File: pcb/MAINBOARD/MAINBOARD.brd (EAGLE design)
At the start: 85 x 56 mm, 67 parts, among them Q1 20MHz, SW1 P-DT6E, SW2 P-DT6E, T1 IRMLM0060TRPbF

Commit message: Přidány opravy chyb, které se vyskytly během oživování
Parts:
- added C10, C7: 100n, !discrete:0805
- added C8, C9: 1n, !discrete:0805
- added D7: 1N4148, #PaJa_30:SOD-80
- added R20, R21: 100k, !discrete:0805
- C1, C3: value 100uF/16V -> 100uF
- D2, D3, D4, D5, D6: device led:CHIPLED_0805 -> !opto:LED_0805
- DC1: value DC-DC-STEPDOWN -> MP1584
- DZ1: value D -ZENEROVA 3.3V -> BZV55C3.3
- DZ2: value D-ZENEROVA 3.3V -> BZV55C3.3
- R1, R11, R12, R2, R3, R4, R7, R8: device rcl:R0603 -> !discrete:0805
- R10, R14, R16, R17, R18, R19: value 68R -> 330R
- R5: device rcl:M1206 -> !discrete:1206
- R6, R9: value DNP -> 10k
- T1: device transistor:SOT23-EBC -> #TD:NPN-BCE
- moved R10 25.4 mm to (38.1, 20.3), flipped to the top
- moved D1 22.9 mm to (35.6, 20.3), flipped to the top, turned to 90 degrees
- moved R15 3.86 mm to (76.8, 25.4), turned to 180 degrees
- moved C4 3.18 mm to (51.4, 8.89)
- moved C6 2.62 mm to (55.9, 9.53), turned to 180 degrees
- moved R1 1.91 mm to (55.2, 21.6)
- moved R11 1.42 mm to (55.9, 12.1)
- moved D3 1.30 mm to (43.8, 2.92), turned to 0 degrees
- moved D4 1.30 mm to (39.4, 2.92), turned to 0 degrees
- moved D5 1.30 mm to (34.9, 2.92), turned to 0 degrees
- moved D6 1.30 mm to (48.3, 2.92), turned to 0 degrees
- moved D2 1.30 mm to (30.5, 2.92), turned to 0 degrees
- moved R7 1.27 mm to (55.9, 26.7)
- moved T1 0.90 mm to (78.7, 29.2)
- moved B1 0.90 mm to (78.7, 45.7)
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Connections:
- net N$2 renamed B
- removed net N$13: D3.C, R17.2
- removed net N$15: D5.C, R18.2
- removed net N$9: D2.C, R16.2
- new net C: D7.A, SG1.-, T1.C
- new net N$2: D6.A, R19.2
- new net N$7: D2.A, R16.2
- net +3V3: now also C10.2, C9.2, R20.2, R21.2; no longer D2.A, D3.A, D4.A, D5.A, D6.A, SG1.+
- net +5V: now also C7.1, C8.1, D7.K, SG1.+
- net AGND: no longer D1.K
- net GND: now also C10.1, C7.2, C8.2, C9.1, D1.K, D2.K, D3.K, D4.K, D5.K, D6.K
- net GPB5-2: now also R20.1
- net GPB6-2: now also R21.1
- net N$3: now also D3.A, R17.2; no longer SG1.-, T1.C
- net N$4: now also D4.A, R14.2; no longer D6.C, R19.2
- net N$6: now also D5.A, R18.2; no longer D4.C, R14.2
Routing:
- net GND: track 64.3 -> 119.3 mm, vias 7 -> 10
- net +5V: track 162.8 -> 211.3 mm
- net C: track 0.00 -> 8.83 mm
- net GPB7-2: track 86.9 -> 78.2 mm
- net VBATT: track 75.7 -> 70.8 mm
- net N$15: track 3.02 -> 0.00 mm
- net N$9: track 3.02 -> 0.00 mm
- net N$13: track 3.02 -> 0.00 mm
- net XTAL2: track 9.72 -> 12.5 mm
- net N$23: track 2.54 -> 5.08 mm
- net +3V3: track 49.1 -> 51.7 mm, vias 2 -> 4
- net XTAL1: track 6.91 -> 9.27 mm
- net N$3: track 4.41 -> 2.16 mm
- net N$7: track 0.00 -> 2.16 mm
- net N$2: track 0.00 -> 2.16 mm
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
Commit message: Velke upravy pred odeslanim do seriove vyroby
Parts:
- removed DZ1, DZ2: BZV55C3.3, #PaJa_22:SOD-80
- removed T1: IRMLM0060TRPbF, #TD:NPN-BCE
- added D8: BZV55C3.3, !discrete:D_SOD80
- added D9: BZV55V3.3, !discrete:D_SOD80
- added T2: (no value), !transistor:SOT23
- D7: value 1N4148 -> LL4148; device #PaJa_30:SOD-80 -> !diody:D_SOD80
- moved C7 3.42 mm to (33.0, 40.0)
- moved C8 2.01 mm to (31.1, 40.0), turned to 90 degrees
- moved R15 1.91 mm to (78.7, 25.4)
- moved JP25 0.76 mm to (6.99, 21.5)
- moved R1 0.64 mm to (55.9, 21.6)
- moved R2 0.63 mm to (62.2, 21.6)
- moved JP26 0.38 mm to (6.99, 16.1)
- moved Q1 0.38 mm to (53.6, 6.99)
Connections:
- net +5V: now also D7.C; no longer D7.K
- net B: now also T2.1; no longer T1.B
- net C: now also T2.2; no longer T1.C
- net GND: now also D8.A, D9.A, T2.3; no longer DZ1.A, DZ2.A, T1.E
- net SCL: now also D9.C; no longer DZ2.K
- net SDA: now also D8.C; no longer DZ1.K
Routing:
- net SDA: track 118.9 -> 121.5 mm, vias 4 -> 3
- net SCL: track 122.2 -> 124.3 mm
- net GPB7-2: track 78.2 -> 80.1 mm
- net B: track 4.29 -> 3.03 mm
- net TRIG1-PD5-OC0B: track 16.7 -> 15.6 mm
- net +5V: track 211.3 -> 210.3 mm
- net N$5: track 2.54 -> 1.91 mm
- added copper zone on layer 1, net GND
- added copper zone on layer 1, net N$12
- added copper zone on layer 1, net N$16

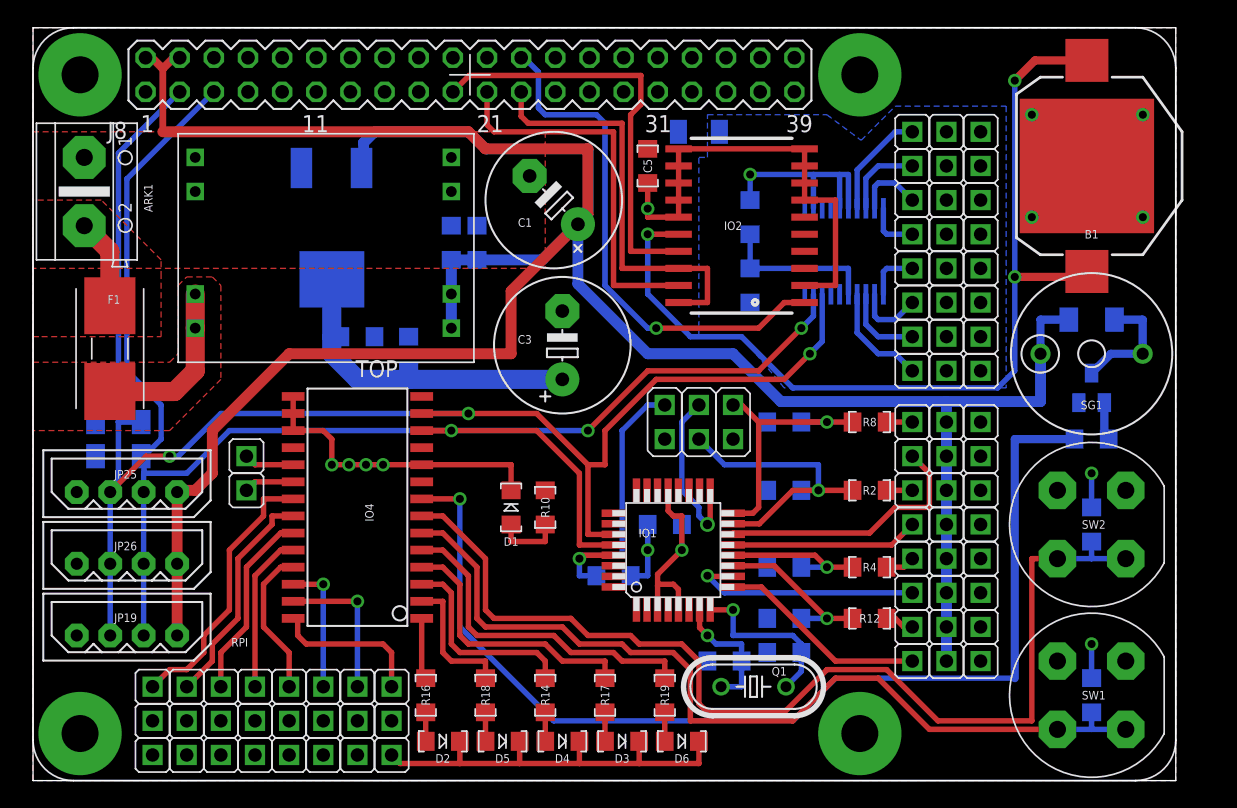
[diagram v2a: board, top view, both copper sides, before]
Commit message: New version of board, shipped to SeedStudio (2x KM2-B, 1x Mainboard -A)
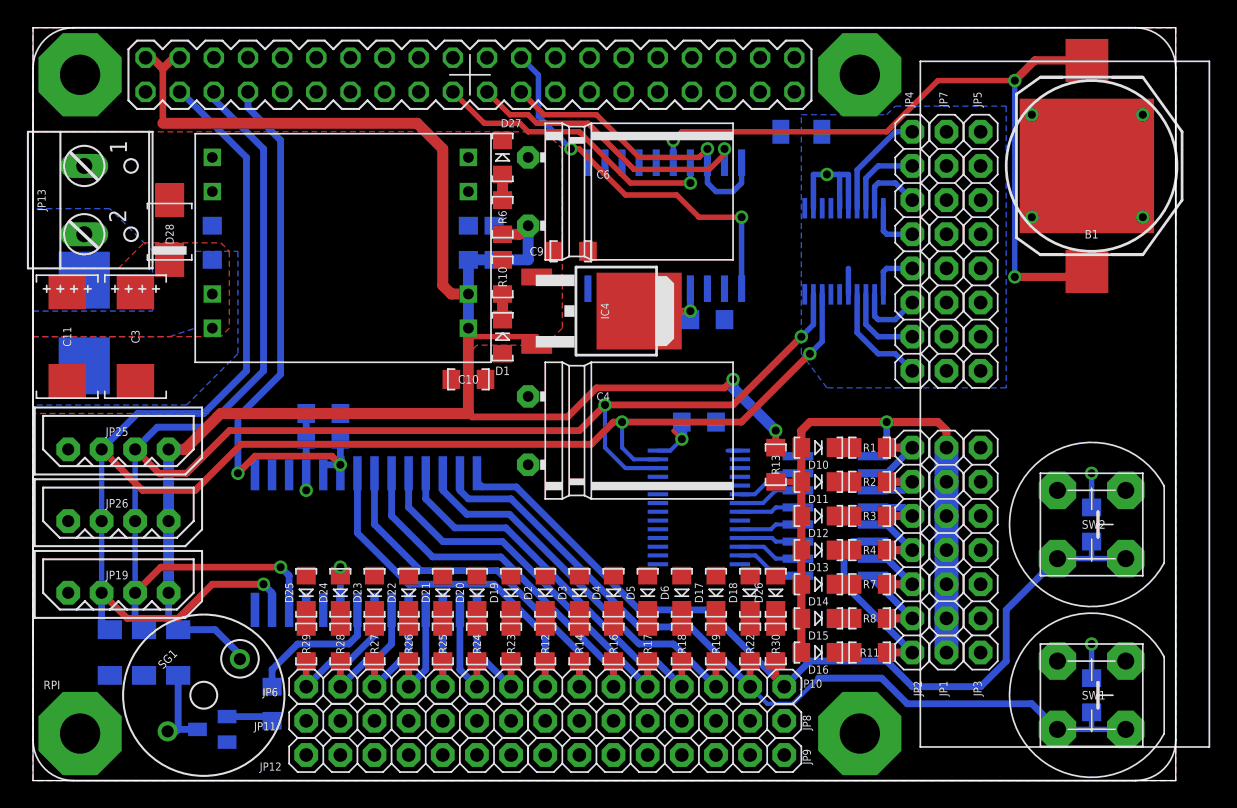
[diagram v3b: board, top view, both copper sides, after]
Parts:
- removed ARK1: ARK500/2, #TD:ARK500/2
- removed IO1: ATmega88PA-AU, !ic_avr:TQFP32
- removed IO4: MCP23017SO, microchip:SO28W
- removed IO5: LD1086, #TD:DPACK
- removed JP14, JP23, JP24, JP28, JP29: S1G8_JUM, #Lamacie lišty by TD:8
- removed Q1: 20MHz, crystal:HC49/S
- added C11: 22M, !discrete:CT7343D
- added C12: 100n, !discrete:0805
- added D10, D11, D12, D13, D14, D15, D16, D17, D18, D19, D20, D21, D22, D23, D24, D25, D26, D27: KP-2012SGC, !opto:LED_0805
- added D28: SK24, !discrete:D_SMB
- added IC1: PCA9685, !ic_nxp:TSSOP28
- added IC2: MCP23017/SO, !ic_microchip:SO28W
- added IC3: ULN2003D1013TR, !uln:SO16
- added IC4: LD1086DT33, !stab:TO252
- added JP12: DS1021-1*8SF1-1, !pinhead:1X07_254_M
- added JP13: TB-5.08-P-2P/BL, !pinhead:1X02_508_SROUB
- added R22, R23, R24, R25, R26, R27, R28, R29, R30: 330, !discrete:0805
- added U$39: (no value), !frames:DIN_A4_SCALE2
- added U$48: (no value), !frames:DIN_DOCFIELD_SCALE2
- C1: value 100uF -> 100n; device rcl:E5-10,5 -> !discrete:0805
- C3: value 100uF -> 22M; device rcl:E5-10,5 -> !discrete:CT7343D
- C4: value 22p -> 1000M; device !discrete:0805 -> !discrete:CE_D10L13_L
- C6: value 22p -> 1000M; device !discrete:0805 -> !discrete:CE_D10L13_R
- D2, D4, D5: value G -> KP-2012SGC
- D3: value O -> KP-2012SGC
- D6: value R -> KP-2012SGC
- D8: value BZV55C3.3 -> BZV55C3V3
- D9: value BZV55V3.3 -> BZV55C3V3
- JP1: value S2G3_JUM -> DS1021-1*8SF1-1; device #Lamacie lišty by TD:2X3 -> !pinhead:1X07_254_M
- JP10, JP4, JP7, JP8, JP9: value S1G3_JUM -> DS1021-1*8SF1-1; device #Lamacie lišty by TD:3 -> !pinhead:1X08_254_M
- JP11, JP2, JP3: value S1G3_JUM -> DS1021-1*8SF1-1; device #Lamacie lišty by TD:3 -> !pinhead:1X07_254_M
- JP5: value S1G8_JUM -> DS1021-1*8SF1-1; device #Lamacie lišty by TD:8 -> !pinhead:1X08_254_M
- JP6: value S1G2_JUM -> DS1021-1*8SF1-1; device #Lamacie lišty by TD:2 -> !pinhead:1X07_254_M
- R1, R11, R3, R7: value 470R -> 330
- R10, R12, R14, R16, R17, R18, R19, R2, R4, R8: value 330R -> 330
- R13: value 10k -> *
- R6: value 10k -> 330
- R9: value 10k -> 100k
- T2: value (none) -> IRLML0060
- moved D7 72.3 mm to (10.8, 9.53), turned to 270 degrees
- moved SG1 70.8 mm to (12.7, 6.35), turned to 45 degrees
- moved T2 70.2 mm to (13.3, 3.81), turned to 270 degrees
- moved R15 64.1 mm to (17.8, 5.71), turned to 270 degrees
- moved JP11 45.8 mm to (27.9, 4.45), turned to 0 degrees
- moved C6 39.2 mm to (36.8, 43.8), flipped to the top, turned to 0 degrees
- moved R9 35.8 mm to (21.6, 25.4), turned to 180 degrees
- moved C3 31.8 mm to (7.62, 33.0), turned to 270 degrees
- moved JP9 30.5 mm to (47.0, 1.91)
- moved C1 25.6 mm to (13.3, 40.0), flipped to the bottom, turned to 90 degrees
- moved JP10 25.5 mm to (47.0, 6.99)
- moved JP8 25.5 mm to (47.0, 4.45)
- moved JP4 25.5 mm to (65.4, 39.4), turned to 90 degrees
- moved R12 24.2 mm to (38.1, 10.2), turned to 90 degrees
- moved JP7 22.9 mm to (67.9, 39.4), turned to 90 degrees
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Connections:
- removed net ECHO1-PD7: IO1.11, R11.2, R12.2
- removed net ECHO2-PB0: IO1.12, R3.2, R4.2
- removed net ECHO3-PB3: IO1.15, JP1.2, R1.2, R2.2
- removed net ECHO4-PB4: IO1.16, JP1.6, R7.2, R8.2
- removed net GPA0-2: IO4.21, JP14.1
- removed net GPA1-2: IO4.22, JP14.2
- removed net GPA2-2: IO4.23, JP14.3
- removed net GPA3-2: IO4.24, JP14.4
- removed net GPA4-2: IO4.25, JP14.5
- removed net GPA5-2: IO4.26, JP14.6
- removed net GPA6-2: IO4.27, JP14.7
- removed net GPA7-2: IO4.28, JP14.8
- removed net GPB0-2: IO4.1, R16.1
- removed net GPB1-2: IO4.2, R18.1
- removed net GPB2-2: IO4.3, R14.1
- removed net GPB3-2: IO4.4, R17.1
- removed net GPB4-2: IO4.5, R19.1
- removed net GPB5-2: IO4.6, R20.1, SW1.2, SW1.2A
- removed net GPB6-2: IO4.7, R21.1, SW2.2, SW2.2A
- removed net GPB7-2: IO4.8, R15.1
- removed net INT/SQW: IO2.5
- removed net INTA1: IO4.20, JP6.2
- removed net INTB1: IO4.19, JP6.1
- removed net N$1: JP11.3, R8.1
- removed net N$11: JP3.3, R12.1
- removed net N$23: D1.A, R10.1
- removed net N$5: JP10.3, R2.1
- removed net N$8: JP7.3, R4.1
- removed net RESET: IO1.29, JP1.4, R13.2
- removed net SCK: IO1.17, JP1.5
- removed net TRIG1-PD5-OC0B: IO1.9, JP2.1
- removed net TRIG2-PD6-OC0A: IO1.10, JP4.1
- removed net TRIG3-PB1-OC1A: IO1.13, JP8.1
- removed net TRIG4-PB2-OC1B: IO1.14, JP9.1
- removed net XTAL1: C4.2, IO1.7, Q1.2
- removed net XTAL2: C6.2, IO1.8, Q1.1
- new net INT: IC2.19, IC2.20, R9.2, RPI.7
- new net LED0: IC1.6, IC3.7
- new net N$17: IC1.7, IC3.6
- new net N$18: D10.A, D11.A, D12.A, D13.A, D14.A, D15.A, D16.A, IC3.9, JP1.1, JP1.2, JP1.3, JP1.4, JP1.5, JP1.6, JP1.7, R13.2
- new net N$19: IC1.8, IC3.5
- new net N$20: D10.K, R1.2
- new net N$21: D16.K, R11.2
- new net N$24: IC1.10, IC3.4
- new net N$25: IC1.11, IC3.3
- new net N$26: IC1.12, IC3.2
- new net N$27: IC1.13, IC3.1
- new net N$28: D15.K, R8.2
- new net N$29: D14.K, R7.2
- new net N$30: D13.K, R4.2
- new net N$31: D12.K, R3.2
- new net N$32: D11.K, R2.2
- new net N$33: D5.K, R17.2
- new net N$34: D4.K, R16.2
- new net N$35: D3.K, R14.2
- new net N$37: D19.K, R23.2
- new net N$38: D25.K, R29.2
- new net N$39: D24.K, R28.2
- new net N$40: D23.K, R27.2
- new net N$41: D22.K, R26.2
- new net N$42: D21.K, R25.2
- new net N$43: D20.K, R24.2
- new net N$9: D27.A, R6.1
- new net PA0: IC2.21, JP10.8, R12.1
- new net PA1: IC2.22, JP10.7, R14.1
- new net PA2: IC2.23, JP10.6, R16.1
- new net PA3: IC2.24, JP10.5, R17.1
- new net PA4: IC2.25, JP10.4, R18.1
- new net PA5: IC2.26, JP10.3, R19.1
- new net PA6: IC2.27, JP10.2, R20.1, R22.1, SW1.2, SW1.2A
- new net PA7: IC2.28, JP10.1, R21.1, R30.1, SW2.2, SW2.2A
- new net PB0: IC2.1, JP6.7, R23.1
- new net PB1: IC2.2, JP6.6, R24.1
- new net PB2: IC2.3, JP6.5, R25.1
- new net PB3: IC2.4, JP6.4, R26.1
- new net PB4: IC2.5, JP6.3, R27.1
- new net PB5: IC2.6, JP6.2, R28.1
- new net PB6: IC2.7, JP6.1, R29.1
- new net PB7: IC2.8, R15.1
- new net PWM0: IC3.10, JP2.1, R1.1
- new net PWM1: IC3.11, JP2.2, R2.1
- new net PWM2: IC3.12, JP2.3, R3.1
- new net PWM4: IC3.13, JP2.4, R4.1
- new net PWM5: IC3.14, JP2.7, R11.1
- new net PWM6: IC3.15, JP2.5, R7.1
- new net PWM7: IC3.16, JP2.6, R8.1
- net +3V3: now also C12.1, C4.P, D1.A, D17.A, D18.A, D19.A, D2.A, D20.A, D21.A, D22.A, D23.A, D24.A, D25.A, D26.A, D3.A, D4.A, D5.A, D6.A, IC1.28, IC2.18, IC2.9, IC4.3, JP11.1, JP11.2, JP11.3, JP11.4, JP11.5, JP11.6, JP11.7, JP7.1, JP7.2, JP7.3, JP7.4, JP7.5, JP7.6, JP7.7, JP7.8, JP8.1, JP8.2, JP8.3, JP8.4, JP8.5, JP8.6, JP8.7, JP8.8, R9.1; no longer C3.+, IO1.1, IO1.18, IO1.19, IO1.2, IO1.20, IO1.22, IO1.23, IO1.24, IO1.25, IO1.26, IO1.30, IO1.31, IO1.32, IO1.4, IO1.6, IO4.18, IO4.9, IO5.4, JP1.3, JP24.1, JP24.2, JP24.3, JP24.4, JP24.5, JP24.6, JP24.7, JP24.8, JP29.1, JP29.2, JP29.3, JP29.4, JP29.5, JP29.6, JP29.7, JP29.8, R10.2, R13.1, R9.2
- net +5V: now also C6.P, IC4.2, R13.1, R6.2; no longer C1.+, IO5.3, JP10.2, JP11.2, JP2.2, JP3.2, JP4.2, JP7.2, JP8.2, JP9.2
- net AD0: now also JP4.8; no longer JP5.1
- net AD1: now also JP4.1; no longer JP5.8
- net AD2: now also JP4.7; no longer JP5.2
- net AD3: now also JP4.2; no longer JP5.7
- net AD4: now also JP4.6; no longer JP5.3
- net AD5: now also JP4.3; no longer JP5.6
- net AD6: now also JP4.5; no longer JP5.4
- net AD7: now also JP4.4; no longer JP5.5
- net AGND: now also IO3.15, JP5.1, JP5.2, JP5.3, JP5.4, JP5.5, JP5.6, JP5.7, JP5.8; no longer JP28.1, JP28.2, JP28.3, JP28.4, JP28.5, JP28.6, JP28.7, JP28.8, R6.2
- net GND: now also C1.2, C11.-, C12.2, C4.M, C6.M, D27.K, D28.A, IC1.1, IC1.14, IC1.2, IC1.23, IC1.24, IC1.25, IC1.3, IC1.4, IC1.5, IC2.10, IC2.15, IC2.16, IC2.17, IC3.8, IC4.1, JP12.1, JP12.2, JP12.3, JP12.4, JP12.5, JP12.6, JP12.7, JP13.1, JP3.2, JP3.3, JP3.4, JP3.5, JP3.6, JP3.7, JP9.1, JP9.2, JP9.4, JP9.5, JP9.6, JP9.7, JP9.8, R10.1; no longer ARK1.1, C1.-, C4.1, C6.1, D1.K, D2.K, D3.K, D4.K, D5.K, D6.K, IO1.21, IO1.3, IO1.5, IO4.10, IO4.15, IO4.16, IO4.17, IO5.1, JP1.1, JP10.1, JP11.1, JP2.3, JP23.1, JP23.2, JP23.3, JP23.4, JP23.5, JP23.6, JP23.7, JP23.8, JP4.3, JP7.1, JP8.3, R1.1, R11.1, R3.1, R7.1
- net N$12: now also C1.1, C11.+, C3.+, D28.K
- net N$16: now also JP13.2; no longer ARK1.2
- net N$2: now also D26.K, R30.2; no longer D6.A, R19.2
- net N$22: now also D1.K, R10.2; no longer IO3.15, R6.1, R9.1
- net N$3: now also D2.K, R12.2; no longer D3.A, R17.2
- net N$4: now also D18.K, R22.2; no longer D4.A, R14.2
- net N$6: now also D17.K, R19.2; no longer D5.A, R18.2
- net N$7: now also D6.K, R18.2; no longer D2.A, R16.2
- net SCL: now also IC1.26, IC2.12; no longer IO1.28, IO4.12
- net SDA: now also IC1.27, IC2.13; no longer IO1.27, IO4.13
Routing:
- net GND: track 119.3 -> 16.4 mm, vias 10 -> 4
- net GPB7-2: track 80.1 -> 0.00 mm, vias 1 -> 0
- net GPB6-2: track 78.7 -> 0.00 mm
- net +5V: track 210.3 -> 137.7 mm, vias 0 -> 2
- net GPB5-2: track 66.8 -> 0.00 mm
- net PA7: track 0.00 -> 66.4 mm
- net PA6: track 0.00 -> 62.9 mm
- net N$18: track 0.00 -> 49.8 mm, vias 0 -> 1
- net INT: track 0.00 -> 43.5 mm, vias 0 -> 2
- net PA5: track 0.00 -> 29.5 mm
- net PA4: track 0.00 -> 28.6 mm
- net PA3: track 0.00 -> 27.7 mm
- net PA2: track 0.00 -> 27.6 mm
- net PA1: track 0.00 -> 27.4 mm
- net PA0: track 0.00 -> 27.3 mm
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- added copper zone on layer 16, net N$12
- added copper zone on layer 16, net N$16
- removed copper zone on layer 1, net N$16
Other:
- board text added: "(c) Frantisek Burian"
- board text added: "(c) Tadeas Divacky"
- board text added: "+"
- board text added: "+5V"
- board text added: "-"
- board text added: "2017"
- board text added: "BRNO"
- board text added: "Brno University of Technology"
- board text added: "FEKT"
- board text added: "GND"
- board text added: "KAMbot"
- board text added: "Main driver board"
- board text added: "PA0"
- board text added: "PA1"
- board text added: "PA2"
- board text added: "PA3"
- board text added: "PA4"
- board text added: "PA5"
- board text added: "PA6"
- board text added: "PA7"
- board text added: "PB0"
- board text added: "PB1"
- board text added: "PB2"
- board text added: "PB3"
- board text added: "PB4"
- board text added: "PB5"
- board text added: "PB6"
- board text added: "PB7"
- board text added: "PWM0"
- board text added: "PWM1"
- board text added: "PWM2"
- board text added: "PWM4"
- board text added: "PWM5"
- board text added: "PWM6"
- board text added: "PWM7"
- board text added: "SCL"
- board text added: "SDA"
- board text added: "UAMT"
- board text added: "UAMT FEKT VUT"
- board text added: "rev A"
- board text removed: "B5"
- board text removed: "B6"
- board text removed: "B7"

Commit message: KM2 a MAINBOARD - posledni upravy pred Release
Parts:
- removed IO2: DS3234, SparkFun:DS3234
- removed U$39: (no value), !frames:DIN_A4_SCALE2
- removed U$48: (no value), !frames:DIN_DOCFIELD_SCALE2
- added IC5: DS3234, !ic_maxim:SO20W
- added U$2: (no value), !frames:DIN_A4_1:2
- added U$3: (no value), !frames:RAZITKO_1:2
- added U$4: (no value), !frames:VUT_LOGO
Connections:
- net +3V3: now also IC5.4; no longer IO2.4
- net CE0: now also IC5.1; no longer IO2.1
- net GND: now also IC5.10, IC5.11, IC5.12, IC5.13, IC5.14, IC5.15, IC5.2, IC5.7, IC5.8, IC5.9; no longer IO2.10, IO2.11, IO2.12, IO2.13, IO2.14, IO2.15, IO2.2, IO2.7, IO2.8, IO2.9
- net MISO: now also IC5.19; no longer IO2.19
- net MOSI: now also IC5.17; no longer IO2.17
- net SCLK: now also IC5.18, IC5.20; no longer IO2.18, IO2.20
- net VBATT: now also IC5.16; no longer IO2.16
